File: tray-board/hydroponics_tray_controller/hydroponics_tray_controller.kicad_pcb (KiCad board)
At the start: 2 copper layers, 99.5 x 99.5 mm, 23 parts, among them J1 Jumper, J2 Display_MSP2401_2.4in_Touch, J4 Power_Comms, J5 i2c_Peripherals, J6 1Wire_Peripherals, U1 ESP32, U2 SP3485EN, U3 AMS1117-3.3

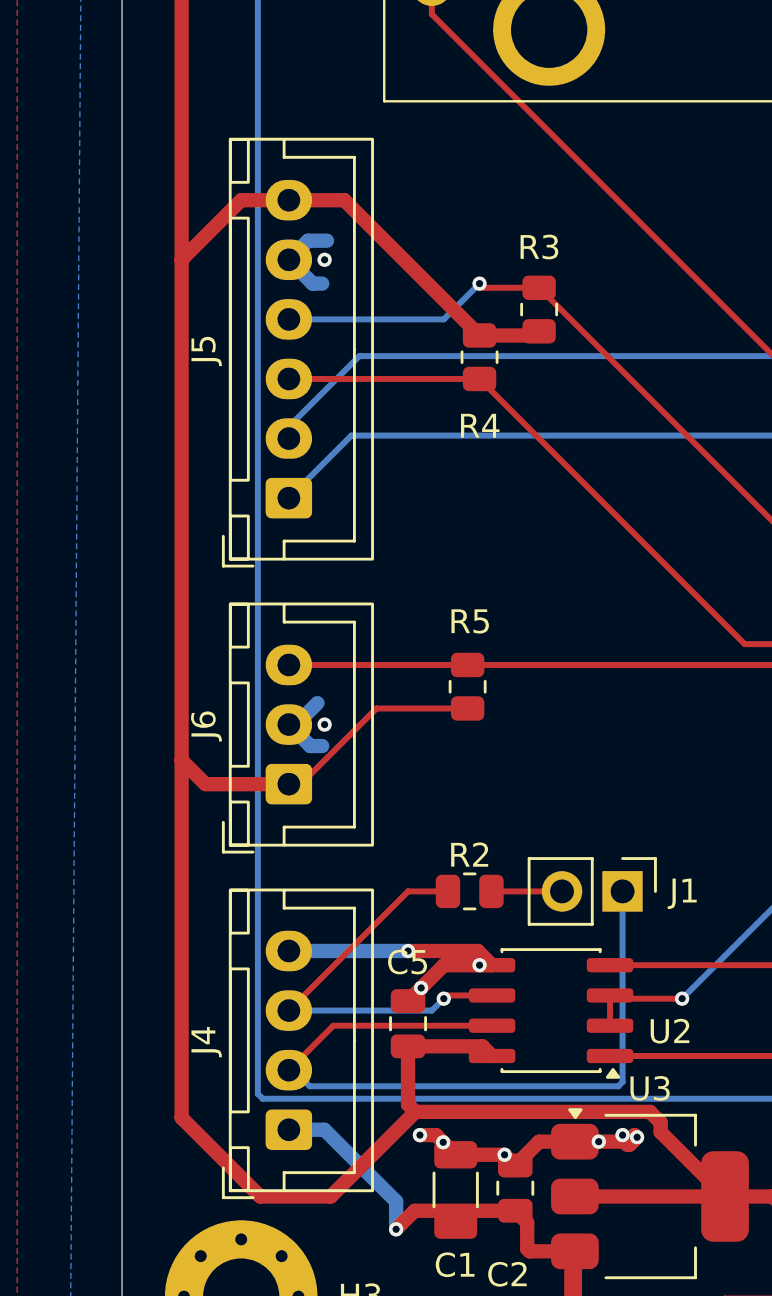
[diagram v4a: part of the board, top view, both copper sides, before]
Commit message: tray-board: connector pinout silkscreen, production release
Add per-pin function labels + connector-name legends on F.Silkscreen for
J4 (Bus: 5V/B/A/GND), J5 (i2c: XS2/XS1/SCL/SDA/GND/3v3), J6 (1Wire:
3V3/GND/DAT) and J1 (RS485 term jumper). Netlist-verified; DRC clean incl.
silk-over-copper. Fab package regenerated via tools/fab.sh (ERC/DRC 0,
BOM all-Basic, CPL 13 placements). Test points deferred to next board.

Co-Authored-By: Claude Sonnet 5 <noreply@anthropic.com>
Claude-Session: https://claude.ai/code/session_018B5wz5uLqNpf9KQR3CBAQm
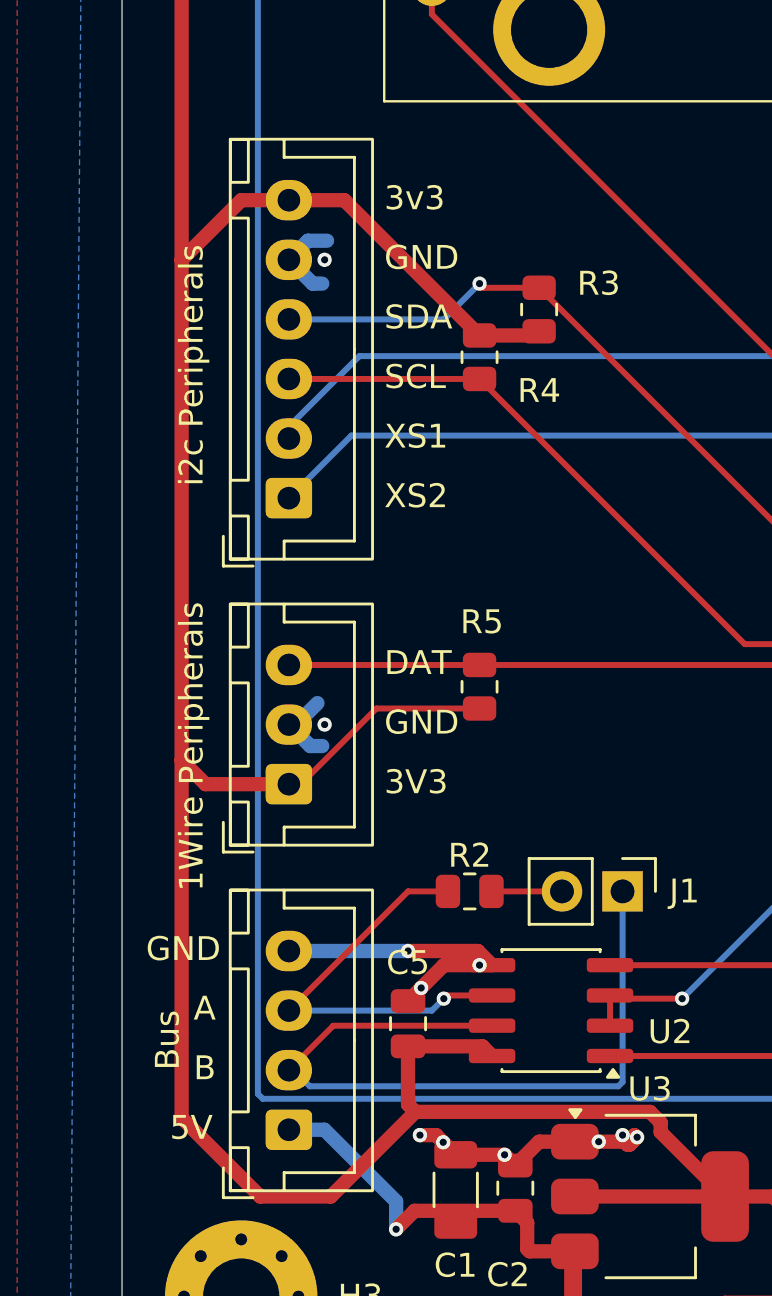
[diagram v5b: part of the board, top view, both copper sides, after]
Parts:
- moved R5 0.50 mm to (35.0, 88.9)
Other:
- board text added: "1Wire Peripherals"
- board text added: "3V3"
- board text added: "3v3"
- board text added: "5V"
- board text added: "A"
- board text added: "B"
- board text added: "Bus"
- board text added: "DAT"
- board text added: "GND"
- board text added: "SCL"
- board text added: "SDA"
- board text added: "XS1"
- board text added: "XS2"
- board text added: "i2c Peripherals"
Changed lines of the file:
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@@
 			(at 3.75 -3.55 90)
 			(layer "F.SilkS")
+			(hide yes)
 			(effects
 				(font
@@
 			(at 3.75 4.6 90)
 			(layer "F.Fab")
+			(hide yes)
 			(effects
 				(font
@@
 		(tags "resistor")
 		(property "Reference" "R3"
-			(at 2.5875 0 180)
+			(at 1.0875 2.5 180)
 			(layer "F.SilkS")
 			(effects
@@
 			(at 2.5 -3.55 90)
 			(layer "F.SilkS")
+			(hide yes)
 			(effects
 				(font
@@
 			(at 2.5 4.6 90)
 			(layer "F.Fab")
+			(hide yes)
 			(effects
 				(font
@@
 		(tags "resistor")
 		(property "Reference" "R4"
-			(at 2.9125 0 0)
+			(at 1.4125 -2.5 0)
 			(layer "F.SilkS")
 			(effects
@@
 	(footprint "Resistor_SMD:R_0805_2012Metric"
 		(layer "F.Cu")
-		(at 34.5 88.9125 90)
+		(at 35 88.9125 90)
 		(descr "Resistor SMD 0805 (2012 Metric), square (rectangular) end terminal, IPC-7351 nominal, (Body size source: IPC-SM-782 page 72, https://www.pcb-3d.com/wordpress/wp-content/uploads/ipc-sm-782a_amendment_1_and_2.pdf)")
 		(tags "resistor")
@@
 			(at 6.25 -3.55 90)
 			(layer "F.SilkS")
+			(hide yes)
 			(effects
 				(font
@@
 			(at 6.25 4.6 90)
 			(layer "F.Fab")
+			(hide yes)
 			(effects
 				(font
@@
 		)
 	)
+	(gr_text "GND"
+		(at 21 100.5 0)
+		(layer "F.SilkS")
+		(effects
+			(font
+				(size 1 1)
+				(thickness 0.1)
+			)
+			(justify left bottom)
+		)
+	)
+	(gr_text "5V"
+		(at 22 108 0)
+		(layer "F.SilkS")
+		(effects
+			(font
+				(size 1 1)
+				(thickness 0.1)
+			)
+			(justify left bottom)
+		)
+	)
+	(gr_text "A"
+		(at 23 103 0)
+		(layer "F.SilkS")
+		(effects
+			(font
+				(size 1 1)
+				(thickness 0.1)
+			)
+			(justify left bottom)
+		)
+	)
+	(gr_text "B"
+		(at 23 105.5 0)
+		(layer "F.SilkS")
+		(effects
+			(font
+				(size 1 1)
+				(thickness 0.1)
+			)
+			(justify left bottom)
+		)
+	)
+	(gr_text "3v3"
+		(at 31 69 0)
+		(layer "F.SilkS")
+		(effects
+			(font
+				(size 1 1)
+				(thickness 0.1)
+			)
+			(justify left bottom)
+		)
+	)
+	(gr_text "GND"
+		(at 31 71.5 0)
+		(layer "F.SilkS")
+		(effects
+			(font
+				(size 1 1)
+				(thickness 0.1)
+			)
+			(justify left bottom)
+		)
+	)
+	(gr_text "SDA"
+		(at 31 74 0)
+		(layer "F.SilkS")
+		(effects
+			(font
+				(size 1 1)
+				(thickness 0.1)
+			)
+			(justify left bottom)
+		)
+	)
+	(gr_text "SCL"
+		(at 31 76.5 0)
+		(layer "F.SilkS")
+		(effects
+			(font
+				(size 1 1)
+				(thickness 0.1)
+			)
+			(justify left bottom)
+		)
+	)
+	(gr_text "XS1"
+		(at 31 79 0)
+		(layer "F.SilkS")
+		(effects
+			(font
+				(size 1 1)
+				(thickness 0.1)
+			)
+			(justify left bottom)
+		)
+	)
+	(gr_text "XS2"
+		(at 31 81.5 0)
+		(layer "F.SilkS")
+		(effects
+			(font
+				(size 1 1)
+				(thickness 0.1)
+			)
+			(justify left bottom)
+		)
+	)
+	(gr_text "DAT"
+		(at 31 88.5 0)
+		(layer "F.SilkS")
+		(effects
+			(font
+				(size 1 1)
+				(thickness 0.1)
+			)
+			(justify left bottom)
+		)
+	)
+	(gr_text "GND"
+		(at 31 91 0)
+		(layer "F.SilkS")
+		(effects
+			(font
+				(size 1 1)
+				(thickness 0.1)
+			)
+			(justify left bottom)
+		)
+	)
+	(gr_text "3V3"
+		(at 31 93.5 0)
+		(layer "F.SilkS")
+		(effects
+			(font
+				(size 1 1)
+				(thickness 0.1)
+			)
+			(justify left bottom)
+		)
+	)
 	(gr_text "Gostwyck Hydroponics\nTray Controller v0.1"
 		(at 74.5 112.5 0)
 		(layer "F.SilkS")
 		(effects
+			(font
+				(size 1 1)
+				(thickness 0.1)
+			)
+			(justify left bottom)
+		)
+	)
+	(gr_text "Bus"
+		(at 22.5 105 90)
+		(layer "F.SilkS")
+		(effects
+			(font
+				(size 1 1)
+				(thickness 0.1)
+			)
+			(justify left bottom)
+		)
+	)
+	(gr_text "i2c Peripherals"
+		(at 23.5 80.5 90)
+		(layer "F.SilkS")
+		(effects
+			(font
+				(size 1 1)
+				(thickness 0.1)
+			)
+			(justify left bottom)
+		)
+	)
+	(gr_text "1Wire Peripherals"
+		(at 23.5 97.5 90)
+		(layer "F.SilkS")
+		(effects
